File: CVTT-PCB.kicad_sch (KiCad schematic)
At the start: 60 parts, among them J1 SERVO1, J2 SERVO2, J3 LCD SCREEN, J4 LCD BUTTONS, J5 Conn_ARM_SWD_TagConnect_TC2030, J6 USB_B_Micro, P2 DC2, P5 DC1, P8 STEPPER, Q7 BSS138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

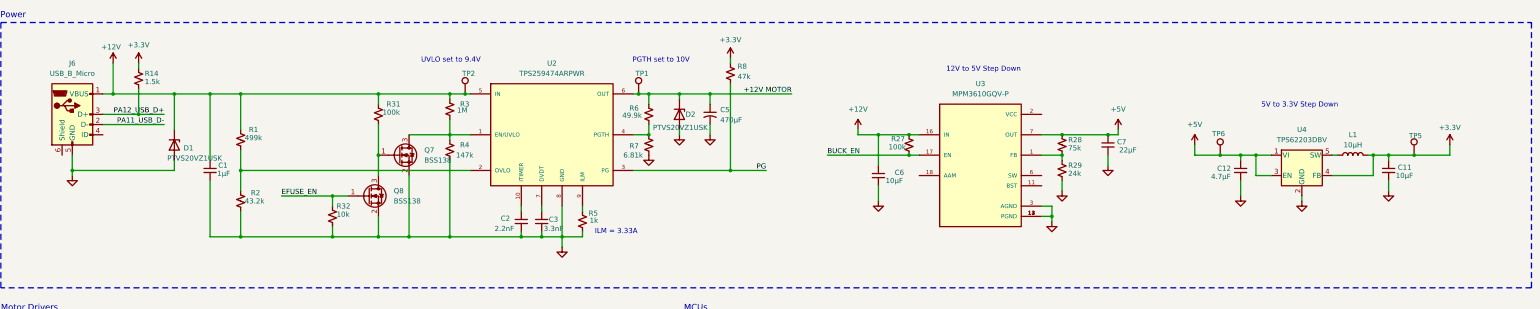
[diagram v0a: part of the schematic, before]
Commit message: Add LED indicators
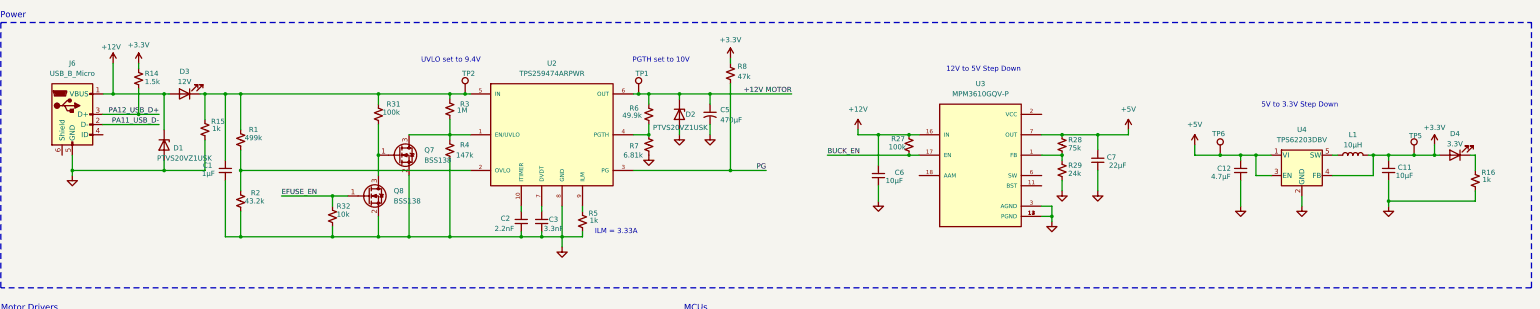
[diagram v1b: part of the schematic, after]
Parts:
- added D3: 12V, LED_SMD:LED_0603_1608Metric, symbol Device:LED
- added D4: 3.3V, LED_SMD:LED_0603_1608Metric, symbol Device:LED
- added R15, R16: 1k, Resistor_SMD:R_0603_1608Metric_Pad0.98x0.95mm_HandSolder, symbol Device:R_Small_US
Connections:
- net +12V: now also D3.2 (A); no longer C1.1, R1.1, R3.1, R31.1, TP2.1, U2.5 (IN)
- net +3.3V: now also D4.2 (A)
- net GND: now also R15.2, R16.2
- new net: C1.1, D3.1 (K), R1.1, R15.1, R3.1, R31.1, TP2.1, U2.5 (IN)
- new net: D4.1 (K), R16.1
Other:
- moved on the sheet: C1, C7, D1

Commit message: Update schem and layout
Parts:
- removed TP1: EFUSE_OUT, TestPoint:TestPoint_Keystone_5000-5004_Miniature, symbol Connector:TestPoint
- removed TP10: GND, TestPoint:TestPoint_Keystone_5000-5004_Miniature, symbol Connector:TestPoint
- removed TP2: EFUSE_IN, TestPoint:TestPoint_Keystone_5000-5004_Miniature, symbol Connector:TestPoint
- removed TP5: +3.3V, TestPoint:TestPoint_Keystone_5000-5004_Miniature, symbol Connector:TestPoint
- removed TP6: +5V, TestPoint:TestPoint_Keystone_5000-5004_Miniature, symbol Connector:TestPoint
- added D5: PG, LED_SMD:LED_0603_1608Metric, symbol Device:LED
- added R17: 53.6k, Resistor_SMD:R_0603_1608Metric_Pad0.98x0.95mm_HandSolder, symbol Device:R_Small_US
- added R18, R19: 10k, Resistor_SMD:R_0603_1608Metric_Pad0.98x0.95mm_HandSolder, symbol Device:R_Small_US
- A2: value Pololu_Breakout_2980 -> POLOLU 2980
- J4: footprint Connector_PinHeader_1.00mm:PinHeader_1x06_P1.00mm_Vertical -> Connector_PinHeader_2.54mm:PinHeader_1x06_P2.54mm_Vertical
- L1: footprint Inductor_SMD:L_0603_1608Metric_Pad1.05x0.95mm_HandSolder -> Inductor_SMD:L_Bourns_SRU5016_5.2x5.2mm
- R8: value 47k -> 3.3k; Manufacturer YAGEO -> (none); Part Number RC0603FR-0747KL -> (none)
- TB1: value Pololu_Breakout_713 -> POLOLU 713
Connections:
- net +3.3V: now also R19.1
- net DRV_EN: now also R19.2
- net GND: now also D5.1 (K), R17.2, R18.2
- net PG: now also D5.2 (A)
- net at U3.18 (AAM): now also R17.1
- net DRV_RST: now reaches A2.13 (~{RESET})
- net DRV_RST: now also U5.41 (PD9); no longer A2.14 (~{SLEEP})
- net DRV_SLEEP: now reaches U5.40 (PD8)
- net DRV_SLEEP: now also A2.14 (~{SLEEP})
- net STBY: now reaches U5.48 (PC8)
- net STBY: now also TB1.13 (~{STBY}), R18.1
- net PMWB: now reaches U5.51 (PD1)
- net PMWB: now also TB1.10 (PWMB)
- net PMWA: now reaches U5.58 (PB4)
- net PMWA: now also TB1.16 (PWMA)
- net BUCK_EN: no longer names the net of R27.2, U3.17 (EN)
- net BUCK_EN: no longer U5.32 (PB12)
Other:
- note added: "MCU/SBCs"
- note removed: "MCUs"
- moved on the sheet: D1, J6

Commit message: Update pinout
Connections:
- net PMWA: now also U5.1 (PC11); no longer U5.58 (PB4)
- net PMWB: now also U5.39 (PC7); no longer U5.51 (PD1)
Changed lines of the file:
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@@
 	(wire
 		(pts
+			(xy 193.04 196.85) (xy 208.28 196.85)
+		)
+		(stroke
+			(width 0)
+			(type default)
+		)
+	)
+	(wire
+		(pts
 			(xy 31.75 135.89) (xy 43.18 135.89)
 		)
@@
 	(wire
 		(pts
-			(xy 264.16 191.77) (xy 279.4 191.77)
-		)
-		(stroke
-			(width 0)
-			(type default)
-		)
-	)
-	(wire
-		(pts
 			(xy 264.16 184.15) (xy 279.4 184.15)
 		)
@@
 	(wire
 		(pts
-			(xy 193.04 156.21) (xy 208.28 156.21)
-		)
-		(stroke
-			(width 0)
-			(type default)
-		)
-	)
-	(wire
-		(pts
 			(xy 64.77 199.39) (xy 80.01 199.39)
 		)
@@
 	(wire
 		(pts
+			(xy 193.04 207.01) (xy 208.28 207.01)
+		)
+		(stroke
+			(width 0)
+			(type default)
+		)
+	)
+	(wire
+		(pts
 			(xy 219.71 127) (xy 219.71 128.27)
 		)
@@
 		)
 	)
+	(label "PMWB"
+		(at 193.04 196.85 0)
+		(effects
+			(font
+				(size 1.27 1.27)
+			)
+			(justify left bottom)
+		)
+	)
 	(label "DRV_RST"
 		(at 193.04 173.99 0)
@@
 		)
 	)
+	(label "PMWA"
+		(at 193.04 207.01 0)
+		(effects
+			(font
+				(size 1.27 1.27)
+			)
+			(justify left bottom)
+		)
+	)
 	(label "STBY"
 		(at 26.67 135.89 0)
@@
 		)
 	)
-	(label "PMWA"
-		(at 279.4 191.77 180)
-		(effects
-			(font
-				(size 1.27 1.27)
-			)
-			(justify right bottom)
-		)
-	)
 	(label "UART_RX"
 		(at 279.4 199.39 180)
@@
 		)
 	)
-	(label "PMWB"
-		(at 193.04 156.21 0)
-		(effects
-			(font
-				(size 1.27 1.27)
-			)
-			(justify left bottom)
-		)
-	)

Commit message: add RGB led status indicator
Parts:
- added D6: STATUS LED, Connector_PinHeader_2.54mm:PinHeader_1x04_P2.54mm_Vertical, symbol Device:LED_KRGB
- added R20: 160, Resistor_SMD:R_0603_1608Metric_Pad0.98x0.95mm_HandSolder, symbol Device:R_Small_US
- added R21, R22: 100, Resistor_SMD:R_0603_1608Metric_Pad0.98x0.95mm_HandSolder, symbol Device:R_Small_US
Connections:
- net GND: now also D6.1 (K)
- net LED_R: now reaches U5.37 (PA9/UCPD1_DBCC1)
- net LED_R: now also R20.2
- net LED_G: now reaches U5.38 (PC6)
- net LED_G: now also R21.2
- net LED_B: now reaches U5.42 (PA10/UCPD1_DBCC2)
- net LED_B: now also R22.2
- new net: D6.2 (RA), R20.1
- new net: D6.3 (GA), R21.1
- new net: D6.4 (BA), R22.1
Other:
- note added: "RGB STATUS LED Description: HS LCA-RGB-10X5-L Part Number: 1082299 Manufacturer: Phoenix Contact"
- title: (none) -> Computer Vision-Based Table Tennis Training System PCB
- moved on the sheet: A2, C1, C10, C11, C12, C13, C2, C3, C4, C5, C6, C7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

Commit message: usb replacement
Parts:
- removed J6: USB_B_Micro, Connector_USB:USB_Micro-B_Wuerth_629105150521, symbol Connector:USB_B_Micro
- removed R14: 1.5k, Resistor_SMD:R_0603_1608Metric_Pad0.98x0.95mm_HandSolder, symbol Device:R_Small_US
- added J7: Barrel_Jack, Local:CUI_PJ-002B, symbol Connector:Barrel_Jack
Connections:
- net +12V: now also J7.1
- net GND: now also J7.2
- net PA11_USB_D-: no longer names the net of U5.43 (PA9/PA11)
- net PA12_USB_D+: no longer names the net of U5.44 (PA10/PA12)
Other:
- moved on the sheet: D1
